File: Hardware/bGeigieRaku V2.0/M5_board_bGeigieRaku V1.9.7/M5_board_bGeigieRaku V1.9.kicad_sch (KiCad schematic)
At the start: 27 parts, among them J1 M5 2x15 pin, J10 QI GND, J11 QI charger Plus, J2 Geiger, J3 GPS, J4 Geiger 2, J5 Extra support header, J7 Conn_01x14_Female, J8 QI charger GND, J9 QI Plus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

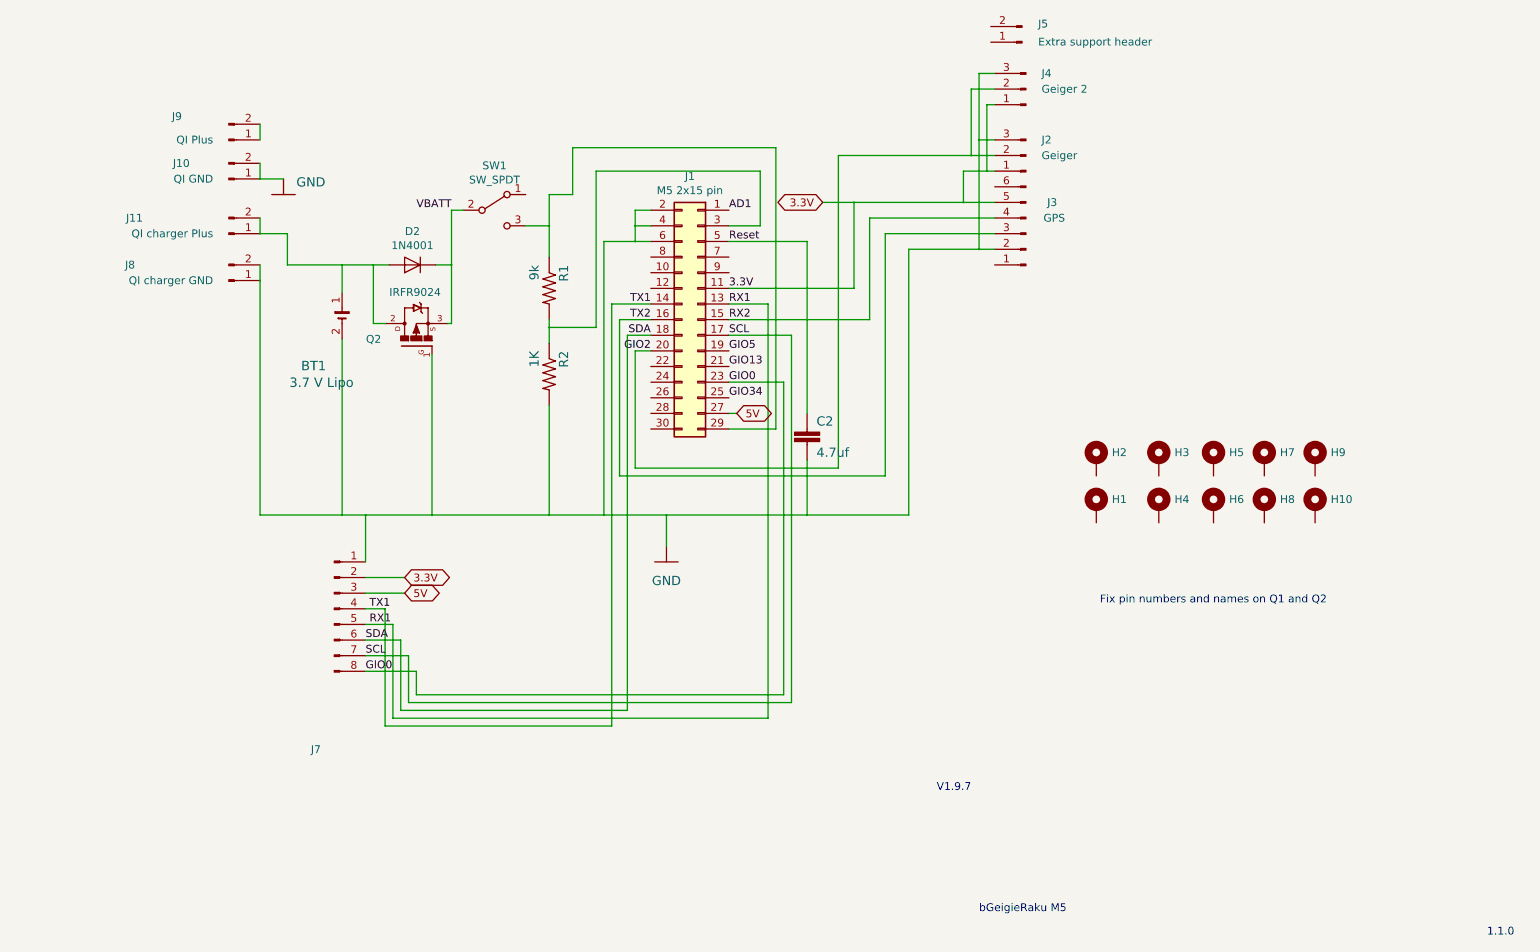
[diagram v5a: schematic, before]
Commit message: Removed extra connectorand diode.  moved MOSFET.
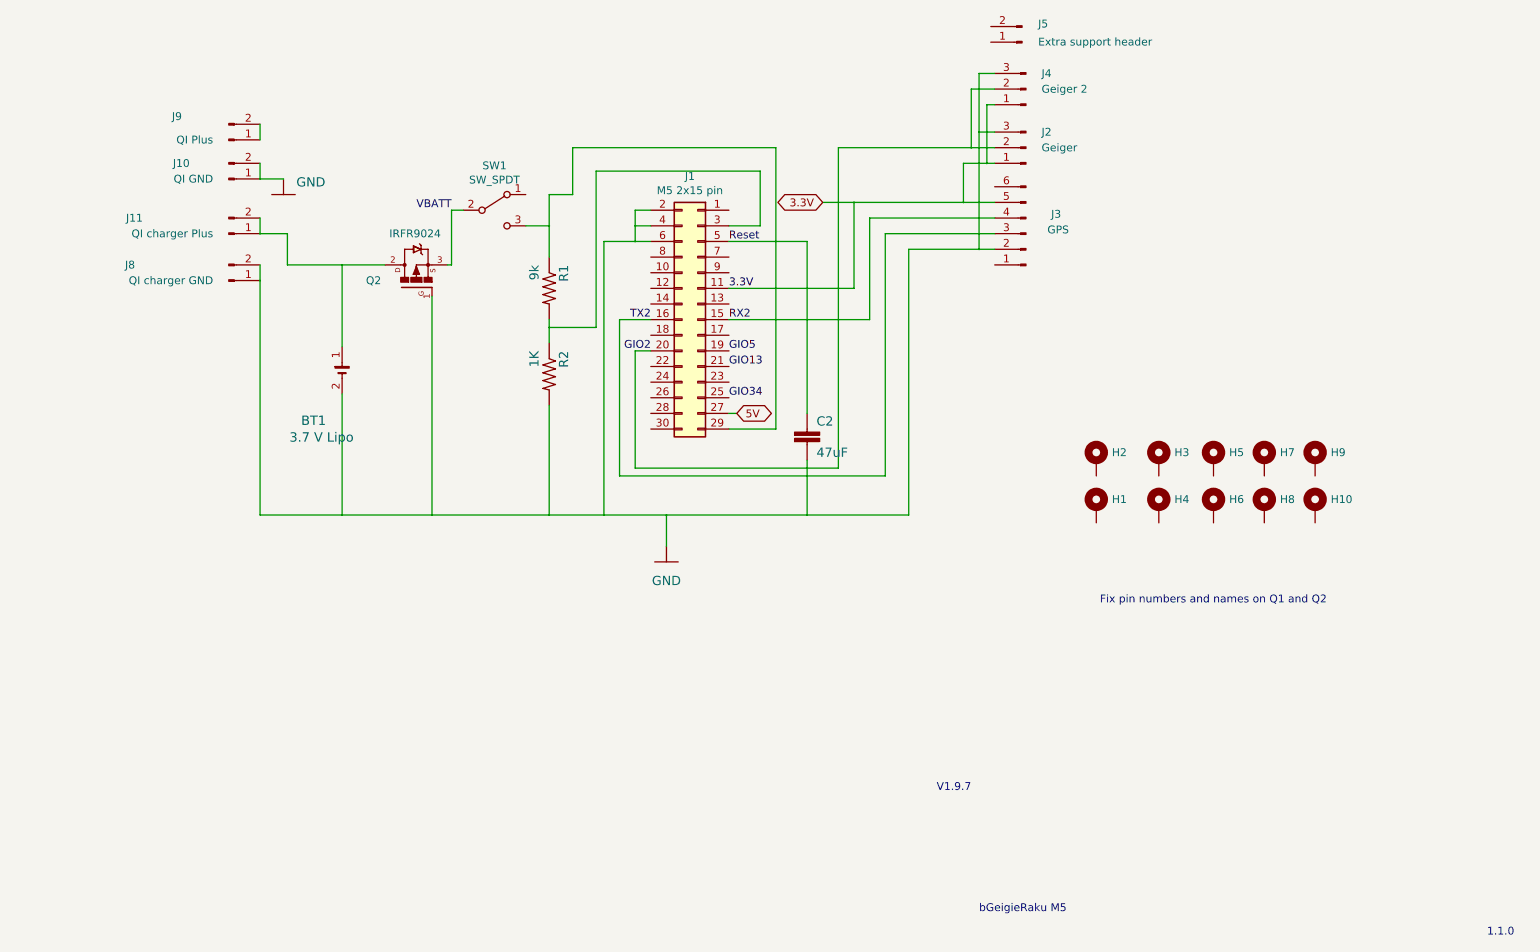
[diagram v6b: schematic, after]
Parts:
- removed D2: 1N4001, Diode_THT:D_DO-41_SOD81_P10.16mm_Horizontal, symbol Diode:1N4001
- removed J7: Conn_01x14_Female, Connector_PinHeader_2.54mm:PinHeader_1x10_P2.54mm_Vertical, symbol Connector:Conn_01x08_Male
- BT1: footprint Battery_Holders:BATTERY_18650-HOLDER -> Library:BATTERY_18650-HOLDER
- C2: value 4.7uf -> 47uF
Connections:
- net AD1: no longer names the net of J1.1 (Pin_1)
- net GIO0: no longer names the net of J1.23 (Pin_23)
- net RX1: no longer names the net of J1.13 (Pin_13)
- net SCL: no longer names the net of J1.17 (Pin_17)
- net SDA: no longer names the net of J1.18 (Pin_18)
- net TX1: no longer names the net of J1.14 (Pin_14)
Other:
- moved on the sheet: BT1, J2, Q2

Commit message: Updated text on schematic
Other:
- note added: "1.9.8"
- note removed: "1.1.0"
- note removed: "Fix pin numbers and names on Q1 and Q2"
- note removed: "V1.9.7"
- note removed: "bGeigieRaku M5"
- company: (none) -> GitHub link at https://github.com/Safecast/bGeigieZen
- title: (none) -> bGeigieZen V1.9.8
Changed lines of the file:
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@@
   (paper "A4")
   (title_block
-    (date "sam. 04 avril 2015")
+    (title "bGeigieZen V1.9.8")
+    (date "2021-04-04")
+    (company "GitHub link at https://github.com/Safecast/bGeigieZen")
   )
   (junction (at 69.85 71.12) (diameter 0.3048) (color 0 0 0 0))
@@
     (effects (font (size 1.27 1.27)) (justify left bottom))
   )
-  (text "V1.9.7" (at 185.42 170.815 180)
-    (effects (font (size 1.27 1.27)) (justify right bottom))
-  )
-  (text "bGeigieRaku M5" (at 186.69 190.5 0)
+  (text "1.9.8" (at 269.24 194.31 0)
     (effects (font (size 1.27 1.27)) (justify left bottom))
   )
-  (text "Fix pin numbers and names on Q1 and Q2" (at 243.205 140.335 180)
-    (effects (font (size 1.27 1.27)) (justify right bottom))
-  )
-  (text "1.1.0" (at 269.24 194.31 0)
-    (effects (font (size 1.27 1.27)) (justify left bottom))
-  )

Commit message: Adde tube rest platform
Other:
- note added: "G36"
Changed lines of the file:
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@@
-(kicad_sch (version 20210126) (generator eeschema)
+(kicad_sch (version 20210406) (generator eeschema)
   (paper "A4")
   (title_block
@@
     (stroke (width 0) (type solid) (color 0 0 0 0))
   )
+  (text "G36" (at 149.86 78.74 180)
+    (effects (font (size 1.27 1.27)) (justify right bottom))
+  )
   (text "\n" (at 179.07 175.26 0)
